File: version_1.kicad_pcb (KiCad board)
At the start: 2 copper layers, 92 parts, among them M5 Motor_Servo_JR, M6 Motor_Servo_JR, M7 Motor_Servo_JR, M8 Motor_Servo_JR, Q1 AO3400A, Q10 AO3400A, Q11 AO3400A, Q12 AO3400A, Q13 AO3400A, Q14 AO3400A, Q15 AO3400A, Q16 AO3400A, Q17 AO3401A, Q18 AO3401A, Q19 AO3401A, Q2 AO3400A, Q20 AO3401A, Q21 AO3400A, Q22 AO3400A, Q23 AO3400A, Q3 AO3400A, Q4 AO3400A, Q5 AO3400A, Q6 AO3400A, Q7 AO3400A, Q8 AO3400A, Q9 AO3400A, U10 74AHC595, U11 ADP2302ARDZ-5.0, U13 XC6206PxxxMR - C5446, U2 SLM2009, U3 SLM2009, U4 SLM2009, U5 SLM2009, U6 SLM2009, U7 SLM2009, U8 SLM2009, U9 SLM2009

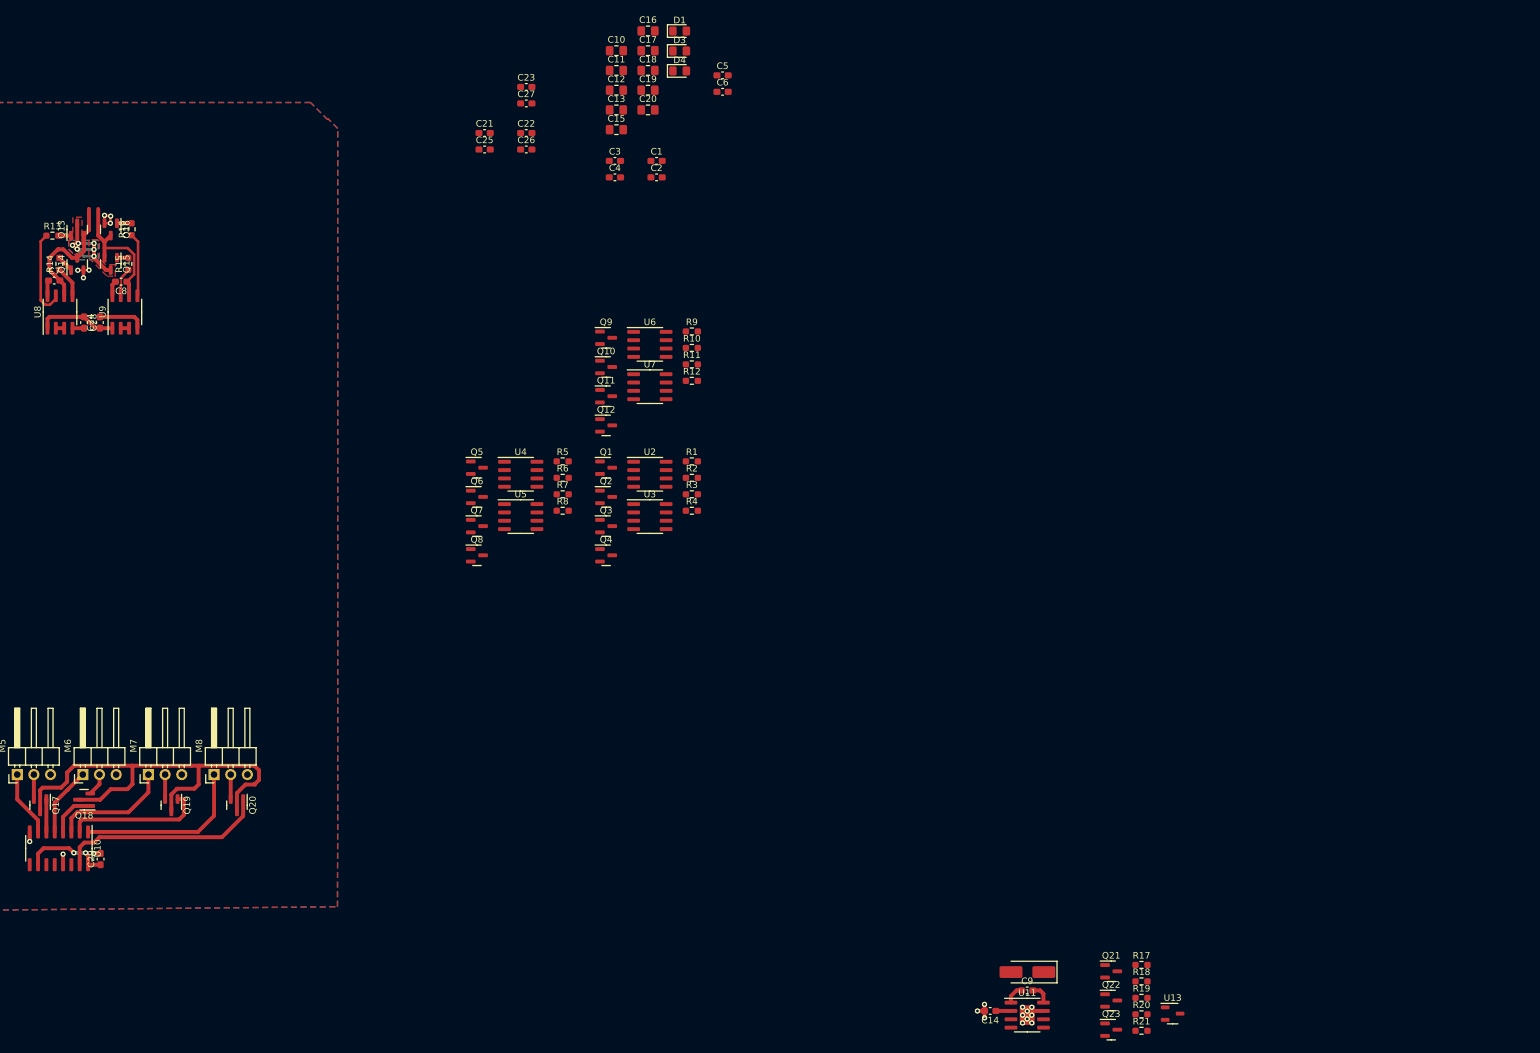
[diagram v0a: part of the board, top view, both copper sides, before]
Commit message: footprint for 18650 holder example pcb battery layout
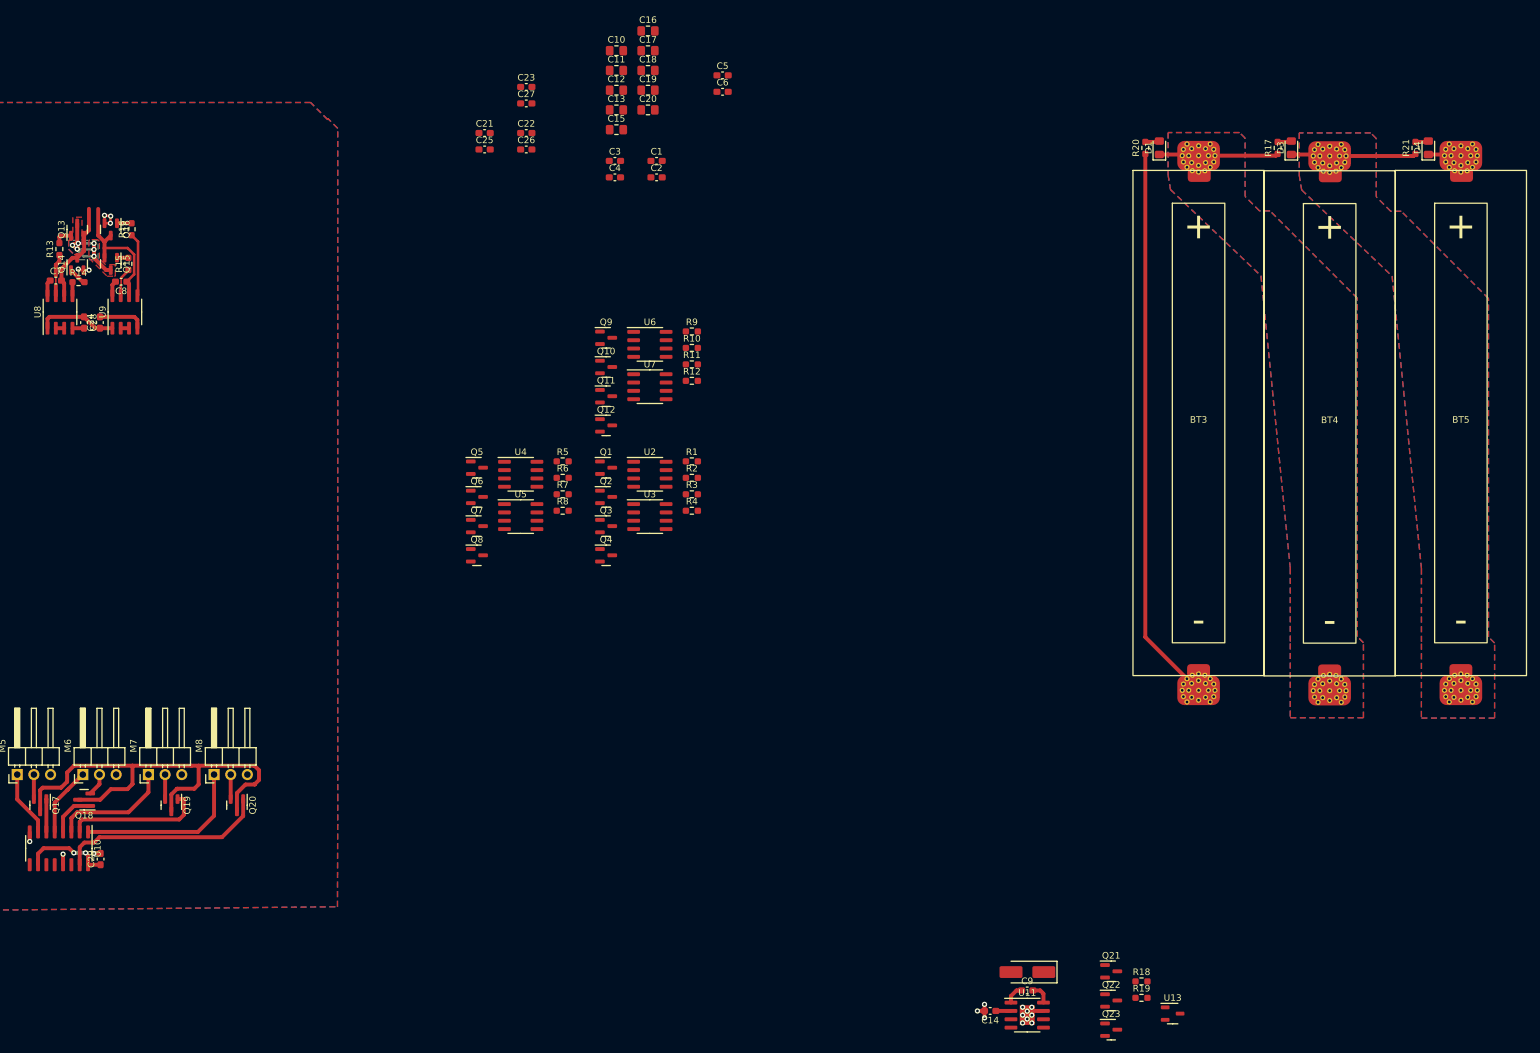
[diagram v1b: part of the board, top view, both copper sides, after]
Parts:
- added BT3: Battery_Cell, 18650:single, F.Cu at (210.1, 65.7)
- added BT4: Battery_Cell, 18650:single, F.Cu at (230.0, 65.8)
- added BT5: Battery_Cell, 18650:single, F.Cu at (250.0, 65.7)
- moved R21 140.9 mm to (243.1, 23.8), turned to 90 degrees
- moved R20 132.1 mm to (201.9, 23.8), turned to 90 degrees
- moved R17 126.2 mm to (222.1, 23.8), turned to 90 degrees
- moved D4 114.7 mm to (245.1, 23.8), turned to 90 degrees
- moved D3 94.4 mm to (224.2, 23.8), turned to 90 degrees
- moved D1 75.3 mm to (204.1, 23.8), turned to 90 degrees
- moved R14 4.03 mm to (39.3, 44.3), turned to 0 degrees
- moved R13 2.30 mm to (36.4, 39.2), turned to 90 degrees
- moved C7 0.24 mm to (35.9, 44.0)
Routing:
- net Net-(BT3--): track 0.00 -> 85.1 mm
- net Net-(BT4-+): track 0.00 -> 19.1 mm
- net Net-(BT3-+): track 0.00 -> 15.7 mm
- net Net-(U8-HO): track 13.7 -> 6.42 mm
- net Net-(J4-Pin_6): track 20.3 -> 15.7 mm
- net Net-(U8-LO): track 4.79 -> 2.07 mm
- net VCC: track 28.3 -> 30.8 mm
- net Net-(D1-A): track 0.00 -> 2.20 mm
- net Net-(D3-A): track 0.00 -> 2.15 mm
- net Net-(D4-A): track 0.00 -> 2.02 mm
- net GND: track 26.8 -> 25.6 mm, vias 20 -> 19
- net Net-(Q13-G): track 1.92 -> 2.79 mm
- added copper zone on B.Cu, net Net-(BT3-+)
- added copper zone on F.Cu, net Net-(BT3-+)
- added copper zone on B.Cu, net Net-(BT4-+)
- added copper zone on F.Cu, net Net-(BT4-+)

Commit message: more capacitance near motors 16x22uF total 3S->2S
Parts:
- removed BT5: Battery_Cell, 18650:single
- removed D4: WRONG!, Diode_SMD:D_0805_2012Metric_Pad1.15x1.40mm_HandSolder
- removed R21: 1k, Resistor_SMD:R_0603_1608Metric_Pad0.98x0.95mm_HandSolder
- added C30: 22u, Capacitor_SMD:C_0805_2012Metric_Pad1.18x1.45mm_HandSolder, F.Cu at (114.4, 52.7)
- added C31: 22u, Capacitor_SMD:C_0805_2012Metric_Pad1.18x1.45mm_HandSolder, F.Cu at (114.4, 50.6)
- added C32: 22u, Capacitor_SMD:C_0805_2012Metric_Pad1.18x1.45mm_HandSolder, F.Cu at (40.1, 30.3)
- added C33: 22u, Capacitor_SMD:C_0805_2012Metric_Pad1.18x1.45mm_HandSolder, F.Cu at (43.1, 29.4)
- added C34: 22u, Capacitor_SMD:C_0805_2012Metric_Pad1.18x1.45mm_HandSolder, F.Cu at (43.1, 31.4)
- added C35: 22u, Capacitor_SMD:C_0805_2012Metric_Pad1.18x1.45mm_HandSolder, F.Cu at (42.4, 35.6)
- added C36: 22u, Capacitor_SMD:C_0805_2012Metric_Pad1.18x1.45mm_HandSolder, F.Cu at (50.6, 40.9)
- added C37: 22u, Capacitor_SMD:C_0805_2012Metric_Pad1.18x1.45mm_HandSolder, F.Cu at (68.6, 40.9)
- added C38: 22u, Capacitor_SMD:C_0805_2012Metric_Pad1.18x1.45mm_HandSolder, F.Cu at (86.6, 40.9)
- added C39: 22u, Capacitor_SMD:C_0805_2012Metric_Pad1.18x1.45mm_HandSolder, F.Cu at (32.6, 40.9)
- added C40: 22u, Capacitor_SMD:C_0805_2012Metric_Pad1.18x1.45mm_HandSolder, F.Cu at (78.5, 33.3)
- added C41: 22u, Capacitor_SMD:C_0805_2012Metric_Pad1.18x1.45mm_HandSolder, F.Cu at (76.1, 30.2)
- added C42: 22u, Capacitor_SMD:C_0805_2012Metric_Pad1.18x1.45mm_HandSolder, F.Cu at (79.1, 29.3)
- added C43: 22u, Capacitor_SMD:C_0805_2012Metric_Pad1.18x1.45mm_HandSolder, F.Cu at (79.1, 31.3)
- added C44: 22u, Capacitor_SMD:C_0805_2012Metric_Pad1.18x1.45mm_HandSolder, F.Cu at (78.3, 35.5)
- added C45: 22u, Capacitor_SMD:C_0805_2012Metric_Pad1.18x1.45mm_HandSolder, F.Cu at (60.6, 33.4)
- added C46: 22u, Capacitor_SMD:C_0805_2012Metric_Pad1.18x1.45mm_HandSolder, F.Cu at (58.2, 30.3)
- added C47: 22u, Capacitor_SMD:C_0805_2012Metric_Pad1.18x1.45mm_HandSolder, F.Cu at (61.2, 29.4)
- added C48: 22u, Capacitor_SMD:C_0805_2012Metric_Pad1.18x1.45mm_HandSolder, F.Cu at (61.2, 31.4)
- added C49: 22u, Capacitor_SMD:C_0805_2012Metric_Pad1.18x1.45mm_HandSolder, F.Cu at (60.4, 35.6)
- added D5: C145232, Diode_SMD:D_SMA_Handsoldering, F.Cu at (130.8, 80.6)
- added D6: C2843868, LED_SMD:LED_RGB_5050-6, F.Cu at (-21.5, 106.3)
- added F1: DFN, Fuse:Fuse_1210_3225Metric_Pad1.42x2.65mm_HandSolder, F.Cu at (-22.7, 113.7)
- added H1: MountingHole, MountingHole:MountingHole_3.2mm_M3, F.Cu at (98.3, 44.5)
- added H2: MountingHole, MountingHole:MountingHole_3.2mm_M3, F.Cu at (28.9, 131.7)
- added H3: MountingHole, MountingHole:MountingHole_3.2mm_M3, F.Cu at (28.8, 51.4)
- added J1: motor_connector, Connector_PinSocket_2.54mm:PinSocket_1x06_P2.54mm_Vertical, F.Cu at (56.6, 26.0)
- added J2: motor_connector, Connector_PinSocket_2.54mm:PinSocket_1x06_P2.54mm_Vertical, F.Cu at (74.6, 26.0)
- added J3: motor_connector, Connector_PinSocket_2.54mm:PinSocket_1x06_P2.54mm_Vertical, F.Cu at (92.6, 26.0)
- added J4: motor_connector, Connector_PinSocket_2.54mm:PinSocket_1x06_P2.54mm_Vertical, F.Cu at (38.6, 26.0)
- added L1: L, Inductor_SMD:L_Changjiang_FNR5020S, F.Cu at (105.9, 57.9)
- added U1: Pico, MCU_RaspberryPi_and_Boards:RPi_Pico_SMD_TH, F.Cu at (188.6, 67.9)
- moved U13 247.8 mm to (-41.5, 167.1)
- moved C15 235.3 mm to (-38.9, 193.4)
- moved C16 235.3 mm to (-34.0, 178.3)
- moved D3 207.5 mm to (37.5, 114.3), turned to 180 degrees
- moved R17 206.5 mm to (37.5, 116.4), turned to 180 degrees
- moved D1 200.0 mm to (37.5, 134.4), turned to 180 degrees
- moved R20 199.4 mm to (37.5, 136.5), turned to 180 degrees
- moved BT4 156.5 mm to (79.5, 108.4), turned to 90 degrees
- moved BT3 144.9 mm to (79.4, 128.4), turned to 90 degrees
- moved R19 128.4 mm to (118.3, 55.5), turned to 180 degrees
- moved R18 127.7 mm to (118.3, 53.8), turned to 180 degrees
- moved D2 124.8 mm to (101.0, 56.3), turned to 90 degrees
- moved U11 122.4 mm to (112.6, 56.5), turned to 180 degrees
- moved C9 116.4 mm to (112.6, 60.3), turned to 180 degrees
- moved M5 116.4 mm to (99.4, 25.9)
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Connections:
- C11 pad 1: +5V -> VCC
- Q21 pad 1: VCC -> Net-(Q21-G)
- Q22 pad 1: VCC -> Net-(Q21-G)
- Q23 pad 1: VCC -> Net-(Q21-G)
- U10 pad 11: unconnected-(U10-SRCLK-Pad11) -> /PWM_CLK
- U10 pad 12: unconnected-(U10-RCLK-Pad12) -> /PWM_CS
- U10 pad 14: unconnected-(U10-SER-Pad14) -> /PWM_DATA
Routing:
- net VCC: track 30.8 -> 263.6 mm, vias 6 -> 24
- net GND: track 25.6 -> 146.6 mm, vias 19 -> 63
- net +5V: track 95.7 -> 200.8 mm, vias 2 -> 8
- net +3.3V: track 0.00 -> 57.8 mm
- net Net-(J1-Pin_1): track 0.00 -> 29.4 mm
- net Net-(J3-Pin_1): track 0.00 -> 27.8 mm
- net Net-(J2-Pin_1): track 0.00 -> 27.4 mm
- net Net-(J1-Pin_6): track 0.00 -> 24.3 mm
- net /Untitled Sheet6/PWR: track 32.1 -> 8.12 mm
- net Net-(Q21-G): track 0.00 -> 22.1 mm
- net Net-(J2-Pin_6): track 0.00 -> 21.2 mm
- net Net-(J3-Pin_6): track 0.00 -> 21.2 mm
- net /Untitled Sheet6/PWM: track 26.5 -> 9.97 mm
- net /Untitled Sheet5/PWR: track 21.2 -> 6.82 mm
- net Net-(BT3--): track 85.1 -> 99.3 mm
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- removed copper zone on B.Cu, net Net-(BT4-+)
- removed copper zone on F.Cu, net Net-(BT4-+)

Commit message: verison 1.0 just routed
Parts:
- removed U13: XC6206PxxxMR - C5446, Package_TO_SOT_SMD:SOT-23-3
- added D4: PWR, Diode_SMD:D_0805_2012Metric_Pad1.15x1.40mm_HandSolder, F.Cu at (109.2, 79.9)
- added Q24: AO3400A, Package_TO_SOT_SMD:SOT-23, F.Cu at (29.1, 97.4)
- added Q25: AO3400A, Package_TO_SOT_SMD:SOT-23, F.Cu at (29.1, 101.0)
- added R21: 1k, Resistor_SMD:R_0603_1608Metric_Pad0.98x0.95mm_HandSolder, F.Cu at (31.8, 82.1)
- added R22: 1k, Resistor_SMD:R_0603_1608Metric_Pad0.98x0.95mm_HandSolder, F.Cu at (34.3, 82.1)
- added R23: 1k, Resistor_SMD:R_0603_1608Metric_Pad0.98x0.95mm_HandSolder, F.Cu at (39.4, 82.1)
- added R24: 4k, Resistor_SMD:R_0603_1608Metric_Pad0.98x0.95mm_HandSolder, F.Cu at (105.2, 79.9)
- added R25: 1k, Resistor_SMD:R_0603_1608Metric_Pad0.98x0.95mm_HandSolder, F.Cu at (48.1, 55.6)
- added R26: 1k, Resistor_SMD:R_0603_1608Metric_Pad0.98x0.95mm_HandSolder, F.Cu at (45.1, 54.6)
- added R27: 1k, Resistor_SMD:R_0603_1608Metric_Pad0.98x0.95mm_HandSolder, F.Cu at (43.5, 54.6)
- added SW1: SW_SPDT, switches:TSM1x3, F.Cu at (115.4, 74.0)
- added U12: LSM6DS3, Package_LGA:LGA-14_3x2.5mm_P0.5mm_LayoutBorder3x4y, F.Cu at (43.8, 83.5)
- C16: value 22u -> 100n; footprint Capacitor_SMD:C_0805_2012Metric_Pad1.18x1.45mm_HandSolder -> Capacitor_SMD:C_0603_1608Metric_Pad1.08x0.95mm_HandSolder
- R19: value 7k6 -> 4k
- moved C15 164.6 mm to (48.1, 53.7)
- moved F1 141.0 mm to (115.4, 85.1), turned to -90 degrees
- moved U1 132.7 mm to (55.9, 68.4), turned to 90 degrees
- moved C16 125.0 mm to (47.8, 83.8), turned to 90 degrees
- moved D5 97.6 mm to (36.9, 54.3), turned to 0 degrees
- moved Q23 94.1 mm to (29.1, 111.9), turned to 0 degrees
- moved Q22 93.2 mm to (29.1, 104.6), turned to 0 degrees
- moved Q21 92.0 mm to (29.1, 108.2), turned to 0 degrees
- moved R20 86.6 mm to (118.3, 105.5), turned to 90 degrees
- moved D1 83.6 mm to (115.5, 104.6), turned to 0 degrees
- moved D3 80.2 mm to (115.6, 96.2)
- moved R17 80.1 mm to (115.5, 98.2)
- moved D6 50.9 mm to (26.9, 90.7), turned to 90 degrees
- moved BT4 17.8 mm to (74.6, 91.3), turned to -90 degrees
- moved BT3 17.8 mm to (74.6, 111.3), turned to -90 degrees
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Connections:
- C15 pad 1: VCC -> Net-(U1-GPIO28_ADC2)
- C16 pad 1: +3.3V -> +5V
- D6 pad 1: unconnected-(D6-RK-Pad1) -> Net-(D6-BA)
- D6 pad 2: unconnected-(D6-GK-Pad2) -> Net-(D6-GK)
- D6 pad 3: unconnected-(D6-BK-Pad3) -> Net-(D6-BK)
- D6 pad 4: unconnected-(D6-BA-Pad4) -> Net-(D6-BA)
- D6 pad 5: unconnected-(D6-GA-Pad5) -> Net-(D6-BK)
- D6 pad 6: unconnected-(D6-RA-Pad6) -> Net-(D6-GK)
- F1 pad 1: Net-(Q21-G) -> Net-(SW1-C)
- Q21 pad 1: Net-(Q21-G) -> Net-(BT4-+)
- Q22 pad 1: Net-(Q21-G) -> Net-(BT4-+)
- Q23 pad 1: Net-(Q21-G) -> Net-(BT4-+)
- U1 pad 1: unconnected-(U1-GPIO0-Pad1) -> Net-(U1-GPIO0)
- U1 pad 10: /ENCODER7 -> /PWM_DATA
- U1 pad 11: /ML1 -> unconnected-(U1-GPIO8-Pad11)
- U1 pad 12: /MR1 -> /ENCODER8
- U1 pad 14: /ML2 -> /ENCODER1
- U1 pad 15: /MR2 -> /ENCODER2
- U1 pad 16: /ML3 -> /ENCODER3
- U1 pad 17: /MR3 -> /ENCODER4
- U1 pad 19: /ML4 -> /ENCODER5
- U1 pad 2: /PWM_CS -> Net-(U1-GPIO1)
- U1 pad 20: /MR4 -> /ENCODER6
- U1 pad 21: /ENCODER1 -> /MR3
- U1 pad 22: /ENCODER2 -> /ML3
- U1 pad 24: /ENCODER3 -> /MR2
- U1 pad 25: /ENCODER4 -> /ML2
- U1 pad 26: /ENCODER5 -> /MR1
- U1 pad 27: /ENCODER6 -> /ML1
- U1 pad 29: unconnected-(U1-GPIO22-Pad29) -> /ENCODER7
- U1 pad 31: unconnected-(U1-GPIO26_ADC0-Pad31) -> /MR4
- U1 pad 32: unconnected-(U1-GPIO27_ADC1-Pad32) -> /ML4
- U1 pad 34: unconnected-(U1-GPIO28_ADC2-Pad34) -> Net-(U1-GPIO28_ADC2)
- U1 pad 36: unconnected-(U1-3V3-Pad36) -> +3.3V
- U1 pad 4: /PWM_CLK -> Net-(U1-GPIO2)
- U1 pad 5: /PWM_DATA -> unconnected-(U1-GPIO3-Pad5)
- U1 pad 7: unconnected-(U1-GPIO5-Pad7) -> /PWM_CS
- U1 pad 9: /ENCODER8 -> /PWM_CLK
- U2 pad 2: /Untitled Sheet1/left -> /ML2
- U2 pad 3: /Untitled Sheet1/left -> /ML2
- U3 pad 2: /Untitled Sheet1/right -> /MR2
- U3 pad 3: /Untitled Sheet1/right -> /MR2
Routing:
- net /ENCODER8: track 0.00 -> 158.0 mm, vias 0 -> 5
- net VCC: track 263.6 -> 412.0 mm, vias 24 -> 26
- net Net-(BT4-+): track 5.93 -> 149.1 mm, vias 0 -> 10
- net /ENCODER1: track 0.00 -> 134.8 mm, vias 0 -> 5
- net /ENCODER2: track 0.00 -> 127.5 mm, vias 0 -> 5
- net /ENCODER3: track 0.00 -> 108.1 mm, vias 0 -> 4
- net /ENCODER4: track 0.00 -> 100.2 mm, vias 0 -> 4
- net /PWM_CS: track 0.00 -> 94.3 mm, vias 0 -> 2
- net /PWM_DATA: track 0.00 -> 91.4 mm, vias 0 -> 4
- net /PWM_CLK: track 0.00 -> 87.6 mm, vias 0 -> 2
- net /ENCODER5: track 0.00 -> 77.5 mm, vias 0 -> 4
- net /ENCODER7: track 0.00 -> 65.2 mm, vias 0 -> 4
- net /ENCODER6: track 0.00 -> 63.2 mm, vias 0 -> 6
- net +3.3V: track 57.8 -> 94.3 mm, vias 0 -> 7
- net /ML4: track 1.27 -> 36.6 mm
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- added copper zone on F.Cu, net Net-(BT4-+)
- added copper zone on F.Cu, net Net-(SW1-C)
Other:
- board outline added: 98.6 x 99.9 mm
- board text added: "M1"
- board text added: "M2"
- board text added: "M3"
- board text added: "M4"
